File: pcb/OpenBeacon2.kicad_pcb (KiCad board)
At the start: 2 copper layers, 100 x 80 mm, 89 parts, among them J1 Bias V, J10 UART, J11 BNC, J2 PAI+, J3 PAI-, J4 Digital IO, J5 ADC Inputs, J6 SMA, J8 I2C Bus, J9 GND, K1 G5V-1-DC5, K2 G5V-1-DC5, M1 LPF 1, M2 LPF 2, Q1 2N7002, Q2 MMBT4403, Q3 2SK3074, Q4 2N7002, Q5 2N7002, Q6 2N7002, U1 TLV61046A, U2 ASTX-H11-25.000MHZ-T, U3 SN74LVC1G17, U4 SI5351A, U5 MCP4725A1T-E/CH, U6 128x32 OLED, U7 Empyrean, U8 24AA64T

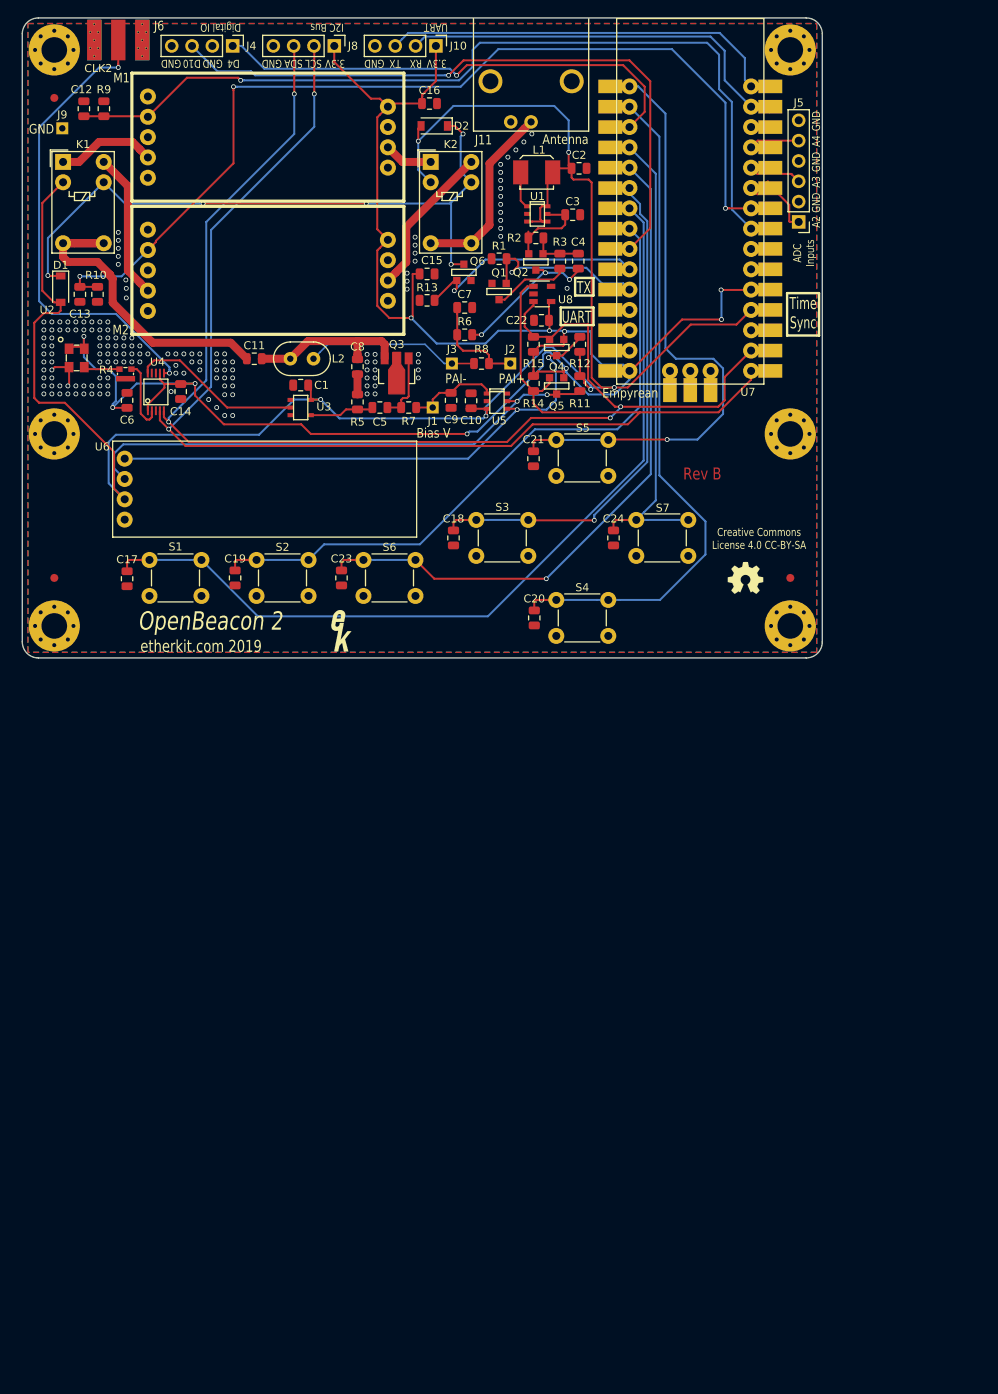
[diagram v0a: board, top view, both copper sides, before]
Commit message: PCB layout pass 1: 100x120 4L outline, JLC 7628 stackup, VFO-pattern mounting holes, placement (no routing)
- Board rebuilt from the merged KiCad 10 schematic (0406853); old KiCad 5 rev B board replaced
- Stackup/rules/RF50 netclass (0.31 mm CPWG, 0.20 gap) from Si5351AVFO pcb-layout
- DS1, S1/S2/S6 at VFO rev4 DS1/SW2/SW3/SW4 positions (+55 mm Y); D-pad cross at VFO encoder area
- RF chain: Si5351/TCXO -> BS170 PA -> K1-K3 -> F2-F5 T30 columns -> K4-K6 -> J11 BNC (right edge)
- CR1220 footprint: locating holes changed to NPTH (were zero-annulus PTH)
- DRC: 0 errors, 0 parity issues; unrouted nets + silkscreen warnings only
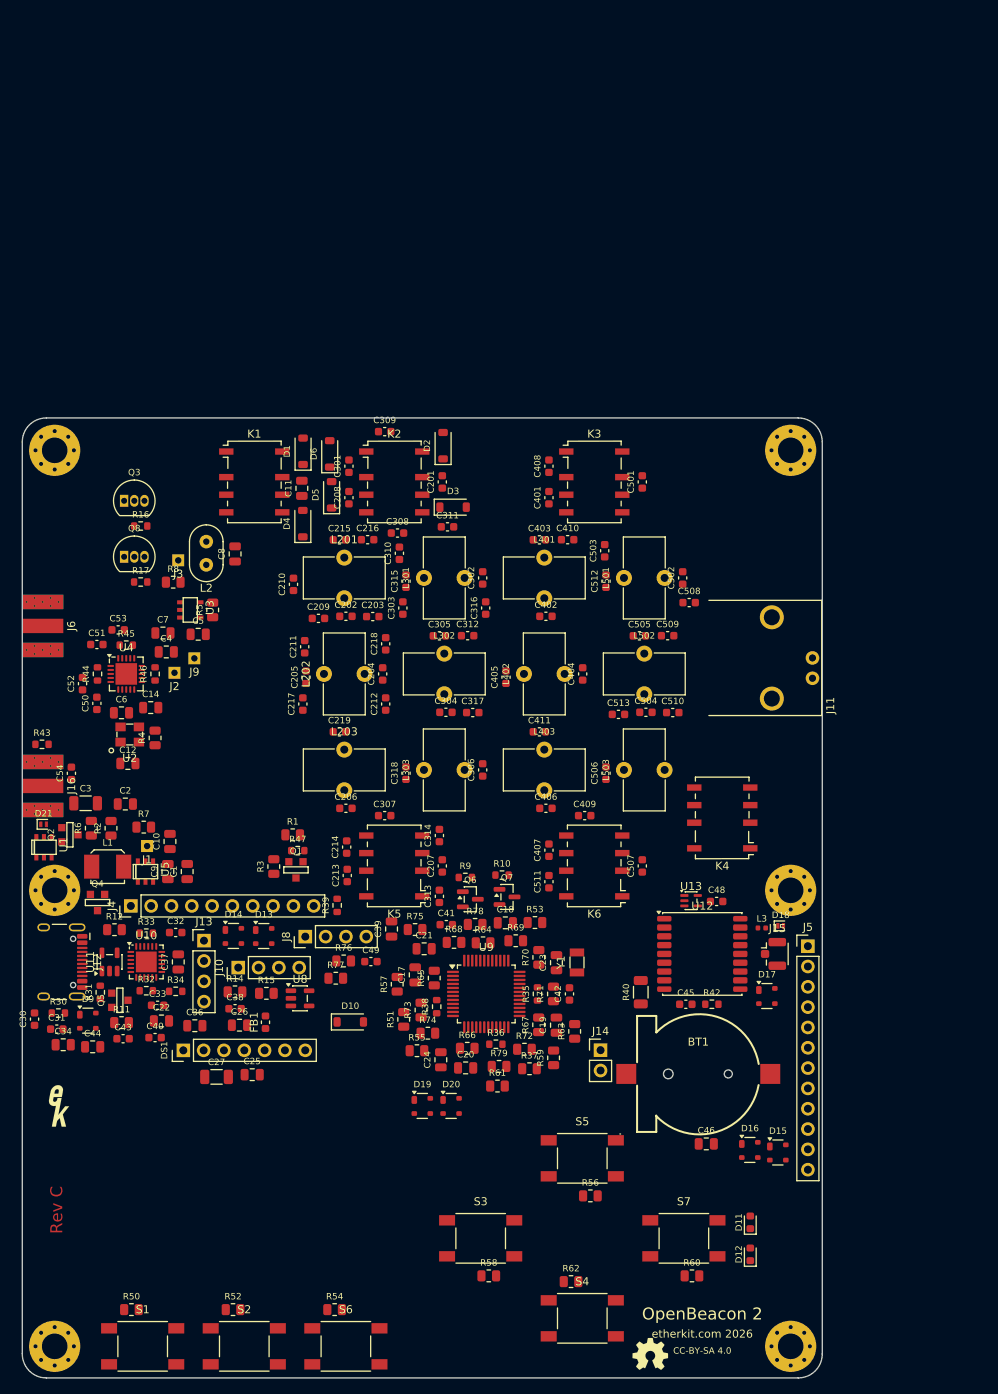
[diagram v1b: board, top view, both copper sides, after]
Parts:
- removed C13: 100n, Capacitor_SMD:C_0805_2012Metric
- removed C15, C16: 4.7u, Capacitor_SMD:C_0805_2012Metric
- removed G***: LOGO, EtherkitKicadLibrary:OSHWLogo4mm
- removed M1: LPF 1, EtherkitKicadLibrary:LPFModule
- removed M2: LPF 2, EtherkitKicadLibrary:LPFModule
- removed R13: 22k, Resistor_SMD:R_0805_2012Metric
- removed REF** (x3): Fiducial_1mm_Dia_2.54mm_Outer_CopperTop, Fiducial:Fiducial_1mm_Dia_2.54mm_Outer_CopperTop
- removed REF** (x6): MountingHole_3.2mm_M3_Pad_Via, MountingHole:MountingHole_3.2mm_M3_Pad_Via
- removed Ref**: Val**, EtherkitKicadLibrary:EtherkitLogoSmall
- removed U6: 128x32 OLED, EtherkitKicadLibrary:128x32OLED
- removed U7: Empyrean, EtherkitKicadLibrary:Empyrean
- added BT1: CR1220, OB2:BAT-SMD_KH-CR1220-2, F.Cu at (184.5, 182.0)
- added C201: 8.2p, Capacitor_SMD:C_0603_1608Metric, F.Cu at (152.5, 108.0)
- added C202: 68p, Capacitor_SMD:C_0603_1608Metric, F.Cu at (140.5, 124.8)
- added C203: 56p, Capacitor_SMD:C_0603_1608Metric, F.Cu at (143.8, 124.8)
- added C204: 100p, Capacitor_SMD:C_0603_1608Metric, F.Cu at (145.1, 132.0)
- added C205: 330p, Capacitor_SMD:C_0603_1608Metric, F.Cu at (135.5, 132.4)
- added C206: 18p, Capacitor_SMD:C_0603_1608Metric, F.Cu at (140.5, 148.8)
- added C207: 100p, Capacitor_SMD:C_0603_1608Metric, F.Cu at (152.5, 156.0)
- added C208: 330p, Capacitor_SMD:C_0603_1608Metric, F.Cu at (140.8, 110.0)
- added C209: 330p, Capacitor_SMD:C_0603_1608Metric, F.Cu at (137.0, 125.1)
- added C210: 330p, Capacitor_SMD:C_0603_1608Metric, F.Cu at (133.9, 120.8)
- added C211: 330p, Capacitor_SMD:C_0603_1608Metric, F.Cu at (135.3, 128.6)
- added C212: 330p, Capacitor_SMD:C_0603_1608Metric, F.Cu at (145.4, 135.8)
- added C213: 100p, Capacitor_SMD:C_0603_1608Metric, F.Cu at (140.6, 157.2)
- added C214: 330p, Capacitor_SMD:C_0603_1608Metric, F.Cu at (140.5, 153.6)
- added C215: 100p, Capacitor_SMD:C_0603_1608Metric, F.Cu at (139.6, 115.2)
- added C216: 330p, Capacitor_SMD:C_0603_1608Metric, F.Cu at (143.2, 115.2)
- added C217: 100p, Capacitor_SMD:C_0603_1608Metric, F.Cu at (135.1, 135.8)
- added C218: 100p, Capacitor_SMD:C_0603_1608Metric, F.Cu at (145.4, 128.2)
- added C219: 68p, Capacitor_SMD:C_0603_1608Metric, F.Cu at (139.6, 139.2)
- added C25: 4.7u, Capacitor_SMD:C_0805_2012Metric, F.Cu at (128.7, 182.1)
- added C26: 4.7u, Capacitor_SMD:C_0805_2012Metric, F.Cu at (127.2, 175.9)
- added C27: 22u, Capacitor_SMD:C_1206_3216Metric, F.Cu at (124.3, 182.4)
- added C30: 100n, Capacitor_SMD:C_0603_1608Metric, F.Cu at (101.5, 175.1)
- added C301: 100p, Capacitor_SMD:C_0603_1608Metric, F.Cu at (140.8, 106.0)
- added C302: 100p, Capacitor_SMD:C_0603_1608Metric, F.Cu at (157.6, 120.0)
- added C303: 56p, Capacitor_SMD:C_0603_1608Metric, F.Cu at (147.6, 123.8)
- added C304: 3p, Capacitor_SMD:C_0603_1608Metric, F.Cu at (153.0, 136.8)
- added C305: 330p, Capacitor_SMD:C_0603_1608Metric, F.Cu at (152.1, 127.2)
- added C306: 12p, Capacitor_SMD:C_0603_1608Metric, F.Cu at (157.6, 144.0)
- added C307: 56p, Capacitor_SMD:C_0603_1608Metric, F.Cu at (145.3, 149.7)
- added C308: 100p, Capacitor_SMD:C_0603_1608Metric, F.Cu at (146.9, 114.4)
- added C309: 100p, Capacitor_SMD:C_0603_1608Metric, F.Cu at (145.3, 101.7)
- added C31: 4.7u, Capacitor_SMD:C_0603_1608Metric, F.Cu at (104.3, 176.4)
- added C310: 100p, Capacitor_SMD:C_0603_1608Metric, F.Cu at (147.1, 116.9)
- added C311: 330p, Capacitor_SMD:C_0603_1608Metric, F.Cu at (153.2, 113.6)
- added C312: 330p, Capacitor_SMD:C_0603_1608Metric, F.Cu at (155.7, 127.2)
- added C313: 100p, Capacitor_SMD:C_0603_1608Metric, F.Cu at (152.1, 159.8)
- added C314: 330p, Capacitor_SMD:C_0603_1608Metric, F.Cu at (152.1, 152.2)
- added C315: 100p, Capacitor_SMD:C_0603_1608Metric, F.Cu at (148.0, 120.4)
- added C316: 100p, Capacitor_SMD:C_0603_1608Metric, F.Cu at (157.9, 123.8)
- added C317: 330p, Capacitor_SMD:C_0603_1608Metric, F.Cu at (156.3, 136.8)
- added C318: 68p, Capacitor_SMD:C_0603_1608Metric, F.Cu at (148.0, 144.4)
- added C32: 100n, Capacitor_SMD:C_0603_1608Metric, F.Cu at (119.2, 164.3)
- added C33: 4.7u, Capacitor_SMD:C_0603_1608Metric, F.Cu at (116.9, 173.4)
- added C34: 1u, Capacitor_SMD:C_0805_2012Metric, F.Cu at (105.1, 178.4)
- added C36: 4.7u, Capacitor_SMD:C_0805_2012Metric, F.Cu at (121.6, 176.0)
- added C37: 100n, Capacitor_SMD:C_0805_2012Metric, F.Cu at (119.5, 168.0)
- added C38: 100n, Capacitor_SMD:C_0603_1608Metric, F.Cu at (126.6, 173.8)
- added C39: 1u, Capacitor_SMD:C_0805_2012Metric, F.Cu at (146.2, 163.9)
- added C40: 100n, Capacitor_SMD:C_0603_1608Metric, F.Cu at (116.6, 177.5)
- added C401: 33p, Capacitor_SMD:C_0603_1608Metric, F.Cu at (165.8, 110.0)
- added C402: 6p, Capacitor_SMD:C_0603_1608Metric, F.Cu at (165.5, 124.8)
- added C403: 330p, Capacitor_SMD:C_0603_1608Metric, F.Cu at (164.6, 115.2)
- added C404: 68p, Capacitor_SMD:C_0603_1608Metric, F.Cu at (170.1, 132.0)
- added C405: 330p, Capacitor_SMD:C_0603_1608Metric, F.Cu at (160.5, 132.4)
- added C406: 3p, Capacitor_SMD:C_0603_1608Metric, F.Cu at (165.5, 148.8)
- added C407: 56p, Capacitor_SMD:C_0603_1608Metric, F.Cu at (165.8, 154.0)
- added C408: 100p, Capacitor_SMD:C_0603_1608Metric, F.Cu at (165.8, 106.0)
- added C409: 100p, Capacitor_SMD:C_0603_1608Metric, F.Cu at (170.3, 149.7)
- added C41: 15p, Capacitor_SMD:C_0603_1608Metric, F.Cu at (153.0, 163.3)
- added C410: 100p, Capacitor_SMD:C_0603_1608Metric, F.Cu at (168.2, 115.2)
- added C411: 68p, Capacitor_SMD:C_0603_1608Metric, F.Cu at (164.6, 139.2)
- added C42: 15p, Capacitor_SMD:C_0603_1608Metric, F.Cu at (168.4, 172.0)
- added C43: 100n, Capacitor_SMD:C_0603_1608Metric, F.Cu at (112.6, 177.6)
- added C44: 4.7u, Capacitor_SMD:C_0805_2012Metric, F.Cu at (108.8, 178.6)
- added C45: 10n, Capacitor_SMD:C_0603_1608Metric, F.Cu at (182.9, 173.3)
- added C46: 1u, Capacitor_SMD:C_0805_2012Metric, F.Cu at (185.5, 190.7)
- added C48: 100n, Capacitor_SMD:C_0603_1608Metric, F.Cu at (186.8, 160.4)
- added C49: 100n, Capacitor_SMD:C_0603_1608Metric, F.Cu at (143.6, 168.0)
- added C50: 100n, Capacitor_SMD:C_0603_1608Metric, F.Cu at (109.3, 135.7)
- added C501: 68p, Capacitor_SMD:C_0603_1608Metric, F.Cu at (177.5, 108.0)
- added C502: 56p, Capacitor_SMD:C_0603_1608Metric, F.Cu at (182.6, 120.0)
- added C503: 68p, Capacitor_SMD:C_0603_1608Metric, F.Cu at (172.8, 116.6)
- added C504: 6.8p, Capacitor_SMD:C_0603_1608Metric, F.Cu at (178.0, 136.8)
- added C505: 22p, Capacitor_SMD:C_0603_1608Metric, F.Cu at (177.1, 127.2)
- added C506: 22p, Capacitor_SMD:C_0603_1608Metric, F.Cu at (173.0, 144.4)
- added C507: 33p, Capacitor_SMD:C_0603_1608Metric, F.Cu at (177.5, 156.0)
- added C508: 100p, Capacitor_SMD:C_0603_1608Metric, F.Cu at (183.4, 123.1)
- added C509: 100p, Capacitor_SMD:C_0603_1608Metric, F.Cu at (180.7, 127.2)
- added C51: 100n, Capacitor_SMD:C_0603_1608Metric, F.Cu at (109.3, 128.3)
- added C510: 100p, Capacitor_SMD:C_0603_1608Metric, F.Cu at (181.3, 136.8)
- added C511: 100p, Capacitor_SMD:C_0603_1608Metric, F.Cu at (165.8, 158.0)
- added C512: 68p, Capacitor_SMD:C_0603_1608Metric, F.Cu at (173.0, 120.4)
- added C513: 68p, Capacitor_SMD:C_0603_1608Metric, F.Cu at (174.5, 137.1)
- added C52: 100n, Capacitor_SMD:C_0603_1608Metric, F.Cu at (107.5, 133.2)
- added C53: 100n, Capacitor_SMD:C_0603_1608Metric, F.Cu at (112.0, 126.5)
- added C54: 100n, Capacitor_SMD:C_0603_1608Metric, F.Cu at (106.1, 144.4)
- added D10: 1N5711W, Diode_SMD:D_SOD-123, F.Cu at (141.0, 175.5)
- added D11: SYNC, LED_SMD:LED_0603_1608Metric, F.Cu at (191.0, 200.6)
- added D12: TX, LED_SMD:LED_0603_1608Metric, F.Cu at (191.0, 204.6)
- added D13: SP0503BAHT, Package_TO_SOT_SMD:SOT-143, F.Cu at (130.2, 164.8)
- added D14: SP0503BAHT, Package_TO_SOT_SMD:SOT-143, F.Cu at (126.4, 164.8)
- added D15: SP0503BAHT, Package_TO_SOT_SMD:SOT-143, F.Cu at (194.4, 191.8)
- added D16: SP0503BAHT, Package_TO_SOT_SMD:SOT-143, F.Cu at (190.9, 191.5)
- added D17: SP0503BAHT, Package_TO_SOT_SMD:SOT-143, F.Cu at (193.1, 172.3)
- added D18: PESD5V0F1BL, Diode_SMD:D_SOD-882, F.Cu at (194.8, 163.5)
- added D19: SP0503BAHT, Package_TO_SOT_SMD:SOT-143, F.Cu at (150.0, 186.0)
- added D20: SP0503BAHT, Package_TO_SOT_SMD:SOT-143, F.Cu at (153.6, 186.0)
- added D21: PESD5V0F1BL, Diode_SMD:D_SOD-882, F.Cu at (102.7, 150.8)
- added D3: 1N4148W, Diode_SMD:D_SOD-123, F.Cu at (153.9, 111.2)
- added D4: 1N4148W, Diode_SMD:D_SOD-123, F.Cu at (135.1, 113.2)
- added D5: 1N4148W, Diode_SMD:D_SOD-123, F.Cu at (138.7, 109.6)
- added D6: 1N4148W, Diode_SMD:D_SOD-123, F.Cu at (138.4, 104.5)
- added D9: SP0503BAHT, Package_TO_SOT_SMD:SOT-143, F.Cu at (108.2, 175.3)
- added DS1: OLED_1.3in_SH1106_SPI_7pin, Connector_PinHeader_2.54mm:PinHeader_1x07_P2.54mm_Vertical, F.Cu at (120.1, 179.1)
- added FB1: BLM18PG221, Inductor_SMD:L_0603_1608Metric, F.Cu at (130.4, 175.5)
- added H1: MountingHole_M3, MountingHole:MountingHole_3.2mm_M3_Pad_Via, F.Cu at (104.0, 159.1)
- added H2: MountingHole_M3, MountingHole:MountingHole_3.2mm_M3_Pad_Via, F.Cu at (196.1, 159.1)
- added H3: MountingHole_M3, MountingHole:MountingHole_3.2mm_M3_Pad_Via, F.Cu at (104.0, 216.1)
- added H4: MountingHole_M3, MountingHole:MountingHole_3.2mm_M3_Pad_Via, F.Cu at (196.1, 216.1)
- added H5: MountingHole_M3, MountingHole:MountingHole_3.2mm_M3_Pad_Via, F.Cu at (104.0, 104.0)
- added H6: MountingHole_M3, MountingHole:MountingHole_3.2mm_M3_Pad_Via, F.Cu at (196.1, 104.0)
- added J12: USB_C_Receptacle, Connector_USB:USB_C_Receptacle_HCTL_HC-TYPE-C-16P-01A, F.Cu at (103.8, 168.0)
- added J13: UPDI, Connector_PinHeader_2.54mm:PinHeader_1x04_P2.54mm_Vertical, F.Cu at (122.7, 165.3)
- added J14: PPS, Connector_PinHeader_2.54mm:PinHeader_1x02_P2.54mm_Vertical, F.Cu at (172.3, 179.0)
- added J15: U.FL, Connector_Coaxial:U.FL_Hirose_U.FL-R-SMT-1_Vertical, F.Cu at (194.4, 167.0)
- added J16: SMA CLKIN, OB2:SMA-ENDLAUNCH, F.Cu at (100.0, 146.0)
- added K3: G6K-2F-Y-DC5, Relay_SMD:Relay_DPDT_Omron_G6K-2F-Y, F.Cu at (171.5, 108.0)
- added K4: G6K-2F-Y-DC5, Relay_SMD:Relay_DPDT_Omron_G6K-2F-Y, F.Cu at (187.5, 150.0)
- added K5: G6K-2F-Y-DC5, Relay_SMD:Relay_DPDT_Omron_G6K-2F-Y, F.Cu at (146.5, 156.0)
- added K6: G6K-2F-Y-DC5, Relay_SMD:Relay_DPDT_Omron_G6K-2F-Y, F.Cu at (171.5, 156.0)
- added L201: 1.10u, Inductor_THT:L_Toroid_Vertical_L10.0mm_W5.0mm_P5.08mm, F.Cu at (140.2, 117.5)
- added L202: 1.55u, Inductor_THT:L_Toroid_Vertical_L10.0mm_W5.0mm_P5.08mm, F.Cu at (137.7, 132.0)
- added L203: 1.90u, Inductor_THT:L_Toroid_Vertical_L10.0mm_W5.0mm_P5.08mm, F.Cu at (140.2, 141.5)
- added L3: 27nH, Inductor_SMD:L_0402_1005Metric, F.Cu at (192.4, 163.8)
- added L301: 430n, Inductor_THT:L_Toroid_Vertical_L10.0mm_W5.0mm_P5.08mm, F.Cu at (150.2, 120.0)
- added L302: 430n, Inductor_THT:L_Toroid_Vertical_L10.0mm_W5.0mm_P5.08mm, F.Cu at (152.8, 129.5)
- added L303: 619n, Inductor_THT:L_Toroid_Vertical_L10.0mm_W5.0mm_P5.08mm, F.Cu at (150.2, 144.0)
- added L401: 292n, Inductor_THT:L_Toroid_Vertical_L10.0mm_W5.0mm_P5.08mm, F.Cu at (165.2, 117.5)
- added L402: 360n, Inductor_THT:L_Toroid_Vertical_L10.0mm_W5.0mm_P5.08mm, F.Cu at (162.7, 132.0)
- added L403: 360n, Inductor_THT:L_Toroid_Vertical_L10.0mm_W5.0mm_P5.08mm, F.Cu at (165.2, 141.5)
- added L501: 130n, Inductor_THT:L_Toroid_Vertical_L10.0mm_W5.0mm_P5.08mm, F.Cu at (175.2, 120.0)
- added L502: 176n, Inductor_THT:L_Toroid_Vertical_L10.0mm_W5.0mm_P5.08mm, F.Cu at (177.8, 129.5)
- added L503: 230n, Inductor_THT:L_Toroid_Vertical_L10.0mm_W5.0mm_P5.08mm, F.Cu at (175.2, 144.0)
- added LOGO1: LOGO, EtherkitKicadLibrary:EtherkitLogoSmall, F.Cu at (104.6, 186.0)
- added LOGO2: LOGO, EtherkitKicadLibrary:OSHWLogo4mm, F.Cu at (178.5, 217.0)
- added Q7: AO3400A, Package_TO_SOT_SMD:SOT-23, F.Cu at (160.6, 159.9)
- added Q8: BS170, Package_TO_SOT_THT:TO-92_Inline, F.Cu at (112.7, 117.4)
- added R16: 10, Resistor_SMD:R_0603_1608Metric, F.Cu at (114.8, 113.5)
- added R17: 10, Resistor_SMD:R_0603_1608Metric, F.Cu at (114.8, 120.5)
- added R30: 5.1k, Resistor_SMD:R_0603_1608Metric, F.Cu at (104.5, 174.4)
- added R31: 5.1k, Resistor_SMD:R_0603_1608Metric, F.Cu at (109.7, 171.8)
- added R32: 1k, Resistor_SMD:R_0603_1608Metric, F.Cu at (115.5, 171.6)
- added R33: 22.1k, Resistor_SMD:R_0603_1608Metric, F.Cu at (115.5, 164.4)
- added R34: 47.5k, Resistor_SMD:R_0603_1608Metric, F.Cu at (119.2, 171.7)
- added R35: 470, Resistor_SMD:R_0603_1608Metric, F.Cu at (164.4, 172.0)
- added R36: 1k, Resistor_SMD:R_0603_1608Metric, F.Cu at (159.2, 178.3)
- added R37: 10k, Resistor_SMD:R_0805_2012Metric, F.Cu at (163.4, 181.4)
- added R38: 470, Resistor_SMD:R_0603_1608Metric, F.Cu at (151.8, 173.6)
- added R39: 470, Resistor_SMD:R_0603_1608Metric, F.Cu at (139.4, 160.9)
- added R40: 10R, Resistor_SMD:R_1206_3216Metric, F.Cu at (177.3, 171.8)
- added R42: 470, Resistor_SMD:R_0603_1608Metric, F.Cu at (186.2, 173.3)
- added R43: 49.9, Resistor_SMD:R_0603_1608Metric, F.Cu at (102.5, 140.8)
- added R44: 10k, Resistor_SMD:R_0603_1608Metric, F.Cu at (109.4, 132.0)
- added R45: 10k, Resistor_SMD:R_0603_1608Metric, F.Cu at (113.0, 128.4)
- added R46: 10k, Resistor_SMD:R_0603_1608Metric, F.Cu at (116.6, 132.0)
- added R47: 33, Resistor_SMD:R_0603_1608Metric, F.Cu at (134.4, 154.1)
- added R50: 10k, Resistor_SMD:R_0805_2012Metric, F.Cu at (113.6, 211.5)
- added R51: 10k, Resistor_SMD:R_0805_2012Metric, F.Cu at (147.7, 175.2)
- added R52: 10k, Resistor_SMD:R_0805_2012Metric, F.Cu at (126.3, 211.5)
- added R53: 10k, Resistor_SMD:R_0805_2012Metric, F.Cu at (164.1, 163.1)
- added R54: 10k, Resistor_SMD:R_0805_2012Metric, F.Cu at (139.0, 211.5)
- added R55: 10k, Resistor_SMD:R_0805_2012Metric, F.Cu at (149.3, 179.1)
- added R56: 10k, Resistor_SMD:R_0805_2012Metric, F.Cu at (171.0, 197.2)
- added R57: 10k, Resistor_SMD:R_0805_2012Metric, F.Cu at (146.9, 170.8)
- added R58: 10k, Resistor_SMD:R_0805_2012Metric, F.Cu at (158.3, 207.2)
- added R59: 10k, Resistor_SMD:R_0805_2012Metric, F.Cu at (166.4, 180.0)
- added R60: 10k, Resistor_SMD:R_0805_2012Metric, F.Cu at (183.7, 207.2)
- added R61: 10k, Resistor_SMD:R_0805_2012Metric, F.Cu at (159.4, 183.5)
- added R62: 10k, Resistor_SMD:R_0805_2012Metric, F.Cu at (168.6, 208.0)
- added R63: 10k, Resistor_SMD:R_0805_2012Metric, F.Cu at (169.0, 176.7)
- added R64: 220R, Resistor_SMD:R_0805_2012Metric, F.Cu at (157.6, 165.6)
- added R65: 220R, Resistor_SMD:R_0805_2012Metric, F.Cu at (151.5, 170.0)
- added R66: 220R, Resistor_SMD:R_0805_2012Metric, F.Cu at (155.6, 178.8)
- added R67: 220R, Resistor_SMD:R_0805_2012Metric, F.Cu at (164.5, 175.9)
- added R68: 220R, Resistor_SMD:R_0805_2012Metric, F.Cu at (154.0, 165.6)
- added R69: 220R, Resistor_SMD:R_0805_2012Metric, F.Cu at (161.7, 165.4)
- added R70: 220R, Resistor_SMD:R_0805_2012Metric, F.Cu at (164.6, 167.4)
- added R71: 220R, Resistor_SMD:R_0805_2012Metric, F.Cu at (166.4, 172.0)
- added R72: 220R, Resistor_SMD:R_0805_2012Metric, F.Cu at (162.8, 178.9)
- added R73: 220R, Resistor_SMD:R_0805_2012Metric, F.Cu at (149.8, 174.0)
- added R74: 220R, Resistor_SMD:R_0805_2012Metric, F.Cu at (150.7, 176.9)
- added R75: 220R, Resistor_SMD:R_0805_2012Metric, F.Cu at (149.1, 164.0)
- added R76: 220R, Resistor_SMD:R_0805_2012Metric, F.Cu at (140.2, 167.9)
- added R77: 220R, Resistor_SMD:R_0805_2012Metric, F.Cu at (139.2, 170.0)
- added R78: 220R, Resistor_SMD:R_0805_2012Metric, F.Cu at (156.6, 163.3)
- added R79: 220R, Resistor_SMD:R_0805_2012Metric, F.Cu at (159.6, 181.1)
- added U10: CP2102N-A02-GQFN24, Package_DFN_QFN:QFN-24-1EP_4x4mm_P0.5mm_EP2.6x2.6mm, F.Cu at (115.5, 168.0)
- added U11: TLV75533PDBV, Package_TO_SOT_SMD:SOT-23-5, F.Cu at (110.9, 168.0)
- added U12: MAX-M10S-00B, RF_GPS:ublox_MAX, F.Cu at (185.0, 167.0)
- added U13: TPS22941, Package_TO_SOT_SMD:SOT-353_SC-70-5, F.Cu at (183.6, 160.3)
- added U9: AVR128DA48-E/PT, Package_QFP:TQFP-48_7x7mm_P0.5mm, F.Cu at (158.0, 172.0)
- added Y1: 32.768kHz, Crystal:Crystal_SMD_3215-2Pin_3.2x1.5mm, F.Cu at (169.3, 168.1)
- C2: value 2.2u -> 4.7u
- C3: footprint Capacitor_SMD:C_0805_2012Metric -> Capacitor_SMD:C_1206_3216Metric
- J4: footprint Connector_PinHeader_2.54mm:PinHeader_1x04_P2.54mm_Vertical -> Connector_PinHeader_2.54mm:PinHeader_1x10_P2.54mm_Vertical
- J5: footprint Connector_PinHeader_2.54mm:PinHeader_1x06_P2.54mm_Vertical -> Connector_PinHeader_2.54mm:PinHeader_1x12_P2.54mm_Vertical
- J6: footprint EtherkitKicadLibrary:SMA-ENDLAUNCH -> OB2:SMA-ENDLAUNCH
- K1, K2: value G5V-1-DC5 -> G6K-2F-Y-DC5; footprint Relay_THT:Relay_SPDT_Omron_G5V-1 -> Relay_SMD:Relay_DPDT_Omron_G6K-2F-Y
- L1: value FDSD0420-H-100M-P3 -> MWSA0402S-100MT
- Q3: value 2SK3074 -> BS170; footprint EtherkitKicadLibrary:SOT89-3 -> Package_TO_SOT_THT:TO-92_Inline
- Q6: value 2N7002 -> AO3400A; footprint EtherkitKicadLibrary:SOT23-2N7002 -> Package_TO_SOT_SMD:SOT-23
- R10, R9: value 270k -> 22k; footprint Resistor_SMD:R_0805_2012Metric -> Resistor_SMD:R_0603_1608Metric
- R4: value PAT1220-C-10dB -> 10; footprint EtherkitKicadLibrary:PAT1220 -> Resistor_SMD:R_0805_2012Metric
- S1, S2, S3, S4, S5, S6, S7: footprint EtherkitKicadLibrary:Omron_B3F-1052 -> OB2:SW_Push_6x6mm_SMD_KH-6X6X11H-STM
- U2: value ASTX-H11-25.000MHZ-T -> 25.000 MHz TCXO
- U4: value SI5351A -> SI5351C-B-GMR; footprint EtherkitKicadLibrary:MSOP-10 -> Package_DFN_QFN:QFN-20-1EP_4x4mm_P0.5mm_EP2.7x2.7mm
- moved J10 117.8 mm to (127.0, 168.7), turned to 90 degrees
- moved J8 111.4 mm to (135.4, 164.8), turned to 90 degrees
- moved J4 108.3 mm to (113.6, 161.0), turned to 90 degrees
- moved R9 106.2 mm to (155.4, 157.4), turned to 0 degrees
- moved L1 102.0 mm to (110.7, 156.1)
- moved U1 100.4 mm to (102.7, 153.7), turned to 0 degrees
- moved C22 99.6 mm to (117.4, 175.4), turned to 0 degrees
- moved R11 98.3 mm to (112.4, 175.6), turned to 0 degrees
- moved C2 97.6 mm to (112.9, 148.3)
- moved S6 96.2 mm to (140.4, 216.1)
- moved S2 96.2 mm to (127.8, 216.1)
- moved S1 96.1 mm to (115.0, 216.1), turned to 0 degrees
- moved C3 95.5 mm to (107.9, 148.2)
- moved Q5 94.2 mm to (112.2, 172.8), turned to 90 degrees
- moved R12 93.5 mm to (111.5, 164.0), turned to 0 degrees
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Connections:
- C11 pad 1: Net-(C11-Pad1) -> /Filter Bank/LPF_IN
- C11 pad 2: Net-(C11-Pad2) -> Net-(Q3-D)
- C12 pad 1: BAND_ID_1 -> Net-(U2-OUT)
- C12 pad 2: GND -> Net-(U4-XA)
- C5 pad 1: Net-(C5-Pad1) -> Net-(C5-~-Pad1)
- C6 pad 1: +3.3V -> Net-(U2-VDD)
- C8 pad 1: Net-(C11-Pad2) -> Net-(Q3-D)
- D1 pad 1: BAND_RELAY -> +5V
- D1 pad 2: +5V -> /Filter Bank/COIL_A
- D2 pad 1: BAND_RELAY -> +5V
- D2 pad 2: +5V -> /Filter Bank/COIL_B
- J10 pad 2: UART_RX -> /I/O + UI/HDR_RX
- J10 pad 3: UART_TX -> /I/O + UI/HDR_TX
- J11 pad 1: Net-(J11-Pad1) -> /Filter Bank/LPF_OUT
- J4 pad 1: D4 -> /I/O + UI/HDR_D7
- J4 pad 3: D10 -> /I/O + UI/HDR_D17
- J5 pad 1: A2 -> /I/O + UI/HDR_D22
- J5 pad 3: A3 -> /I/O + UI/HDR_D23
- J5 pad 5: A4 -> /I/O + UI/HDR_D24
- J6 pad 1: Net-(J6-Pad1) -> Net-(J6-In)
- J8 pad 2: SCL -> /I/O + UI/HDR_SCL
- J8 pad 3: SDA -> /I/O + UI/HDR_SDA
- K1 pad 1: Net-(K1-Pad1) -> +5V
- K1 pad 2: +5V -> /Filter Bank/P1_IN
- K1 pad 5: Net-(C11-Pad1) -> unconnected-(K1-Pad5)
- K1 pad 6: Net-(C11-Pad1) -> unconnected-(K1-Pad6)
- K2 pad 1: Net-(K2-Pad1) -> +5V
- K2 pad 2: +5V -> /Filter Bank/F80_60_IN
- K2 pad 5: Net-(J11-Pad1) -> unconnected-(K2-Pad5)
- K2 pad 6: Net-(J11-Pad1) -> unconnected-(K2-Pad6)
- L2 pad 2: Net-(C11-Pad2) -> Net-(Q3-D)
- Q3 pad 1: GND -> Net-(Q3-D)
- Q3 pad 2: Net-(C5-Pad1) -> Net-(Q3-G)
- Q3 pad 3: Net-(C11-Pad2) -> GND
- Q6 pad 1: GND -> BAND_A
- Q6 pad 2: BAND_SW -> GND
- Q6 pad 3: BAND_RELAY -> /Filter Bank/COIL_A
- R10 pad 1: BAND_ID_2 -> BAND_B
- R4 pad 1: Net-(R4-Pad1) -> +3.3V
- R4 pad 2: Net-(R4-Pad2) -> Net-(U2-VDD)
- R7 pad 1: Net-(C5-Pad1) -> Net-(C5-~-Pad1)
- R9 pad 1: BAND_ID_1 -> BAND_A
- S1 pad 1: BTN_DSP_1 -> GND
- S1 pad 2: BTN_DSP_1 -> Net-(R50-Pad2)
- S2 pad 2: GND -> Net-(R52-Pad2)
- S3 pad 1: BTN_LEFT -> GND
- S3 pad 2: BTN_LEFT -> Net-(R58-Pad2)
- S4 pad 2: GND -> Net-(R62-Pad2)
- S5 pad 2: GND -> Net-(R56-Pad2)
- S6 pad 2: GND -> Net-(R54-Pad2)
- S7 pad 2: GND -> Net-(R60-Pad2)
- U2 pad 1: +3.3V -> GND
- U2 pad 3: Net-(R4-Pad1) -> Net-(U2-OUT)
- U2 pad 4: +3.3V -> Net-(U2-VDD)
- U4 pad 1: +3.3V -> Net-(U4-XA)
- U4 pad 10: CLK0 -> +3.3V
- U4 pad 2: Net-(R4-Pad2) -> unconnected-(U4-XB-Pad2)
- U4 pad 3: Net-(U4-Pad3) -> SI_INTR
- U4 pad 6: Net-(J6-Pad1) -> Net-(U4-CLKIN)
- U4 pad 7: +3.3V -> GND
- U4 pad 8: GND -> unconnected-(U4-CLK3-Pad8)
- U4 pad 9: Net-(U4-Pad9) -> Net-(J6-In)
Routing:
- net +5V: track 245.2 -> 0.00 mm, vias 6 -> 0
- net +3.3V: track 240.6 -> 0.00 mm, vias 10 -> 0
- net SCL: track 171.3 -> 0.00 mm, vias 2 -> 0
- net SDA: track 162.5 -> 0.00 mm, vias 4 -> 0
- net BAND_ID_2: track 122.7 -> 0.00 mm, vias 3 -> 0
- net BTN_DSP_1: track 109.1 -> 0.00 mm
- net BAND_ID_1: track 108.8 -> 0.00 mm, vias 1 -> 0
- net BTN_BACK: track 85.7 -> 0.00 mm, vias 1 -> 0
- net BTN_DOWN: track 84.9 -> 0.00 mm
- net BAND_RELAY: track 82.7 -> 0.00 mm, vias 5 -> 0
- net D10: track 82.7 -> 0.00 mm, vias 1 -> 0
- net BTN_DSP_2: track 82.6 -> 0.00 mm
- net BTN_UP: track 75.6 -> 0.00 mm, vias 1 -> 0
- net SDA_5V: track 69.0 -> 0.00 mm, vias 2 -> 0
- net SCL_5V: track 66.5 -> 0.00 mm, vias 2 -> 0
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- removed copper zone on B.Cu, net GND
- removed copper zone on F.Cu, net GND
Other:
- board size 100 x 80 mm -> 100 x 120 mm
- copper layers 2 -> 4
- net class 50ohm removed
- net class Default removed
- rule pad_to_mask_clearance: 0.2 -> 0
- board text added: "1.3in SH1106 OLED (DS1) - module area: low-profile SMD only, no tall parts"
- board text added: "CC-BY-SA 4.0"
- board text added: "Controlled impedance 50 ohm, L1/L2, 0.31/0.20 (CPWG, RF50) per JLC calculator"
- board text added: "FAB NOTES: JLC04161H-7628 4L 1.6mm, 1oz outer"
- board text added: "Hand solder: J11, L2, Q3, Q8, toroids L201-L503, DS1"
- board text added: "OpenBeacon 2 - NT7S / Etherkit"
- board text added: "PA (Q3/Q8/L2): give drains a dedicated F.Cu+B.Cu heat-spread pour with via stitching (routing pass)"
- board text added: "Rev C"
- board text added: "etherkit.com 2026"
- board text removed: "3.3V"
- board text removed: "A2"
- board text removed: "A3"
- board text removed: "A4"
- board text removed: "ADC Inputs"
- board text removed: "Antenna"
- board text removed: "Bias V"
- board text removed: "CLK2"
- board text removed: "Creative Commons License 4.0 CC-BY-SA"
- board text removed: "D10"
- board text removed: "D4"
- board text removed: "Digital IO"
- board text removed: "Empyrean"
- board text removed: "GND"
- board text removed: "I2C Bus"
- board text removed: "PAI+"
- board text removed: "PAI-"
- board text removed: "RX"
- board text removed: "Rev B"
- board text removed: "SCL"
- board text removed: "SDA"
- board text removed: "TX"
- board text removed: "Time Sync"
- board text removed: "UART"
- board text removed: "etherkit.com 2019"

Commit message: PCB placement: J11 BNC on back edge at filter output, reversed filter bank flow, aligned/labelled header row
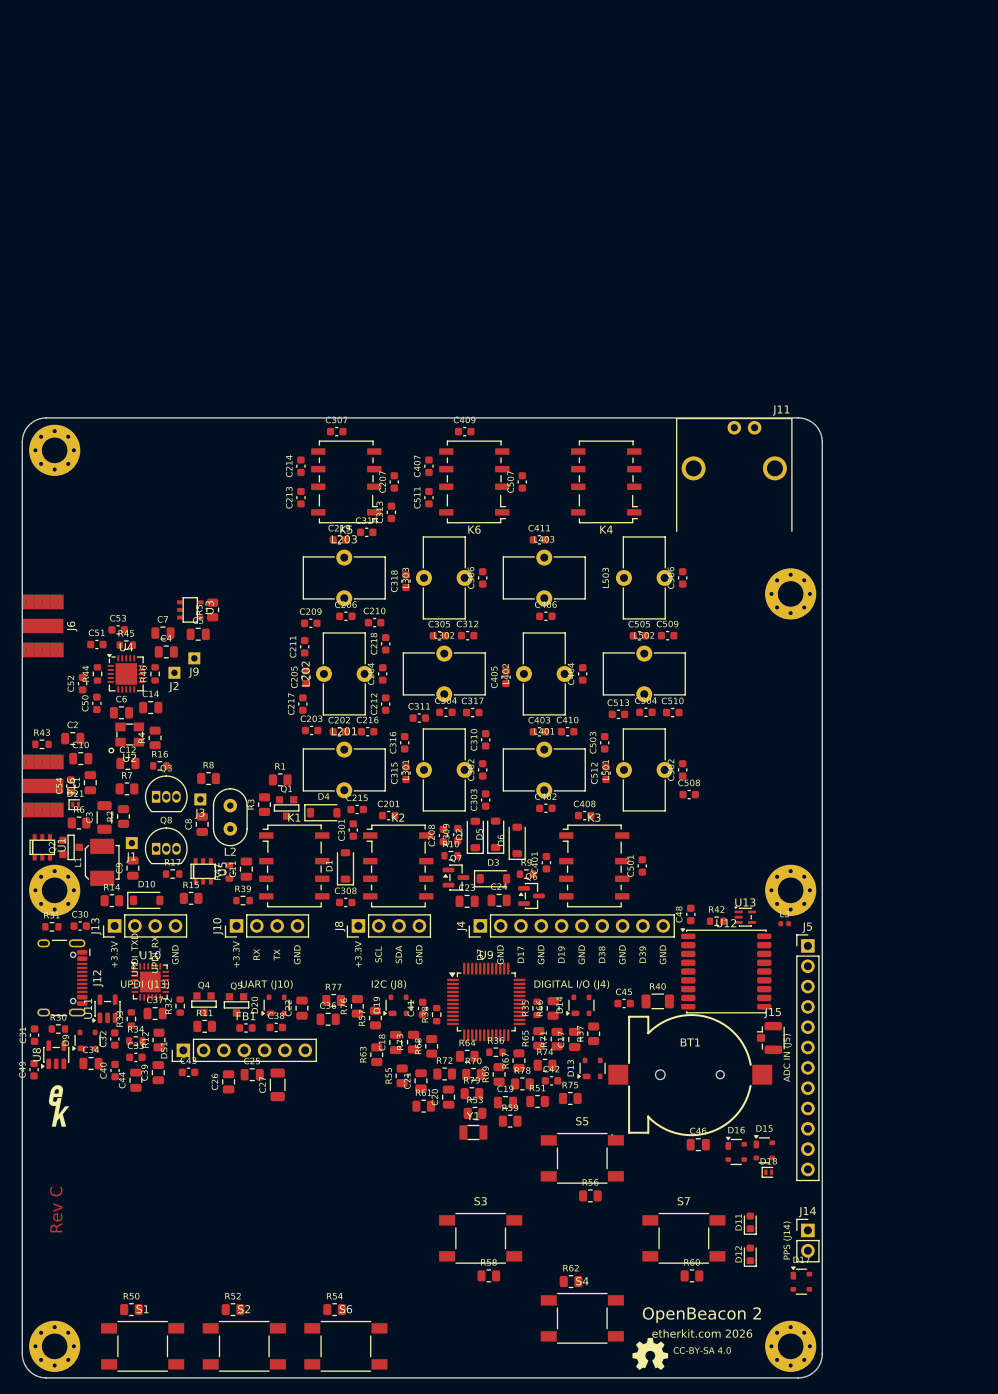
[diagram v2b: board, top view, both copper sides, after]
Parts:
- moved D6 53.7 mm to (161.9, 152.8)
- moved D1 52.1 mm to (140.4, 156.0)
- moved C309 51.2 mm to (154.4, 152.1), turned to 90 degrees
- moved C511 50.3 mm to (150.8, 110.0)
- moved C507 50.3 mm to (162.5, 108.0)
- moved K6 50.3 mm to (156.5, 108.0)
- moved C407 50.3 mm to (150.8, 106.0)
- moved C409 50.3 mm to (155.3, 101.7)
- moved D2 48.8 mm to (156.6, 152.1)
- moved C207 48.4 mm to (146.5, 108.0)
- moved C313 48.4 mm to (146.1, 111.8)
- moved K5 48.4 mm to (140.5, 108.0)
- moved C307 48.4 mm to (139.3, 101.7)
- moved K1 48.3 mm to (134.0, 156.0)
- moved C11 48.1 mm to (128.0, 156.4)
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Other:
- board text added: "+3.3V"
- board text added: "ADC IN (J5)"
- board text added: "D17"
- board text added: "D19"
- board text added: "D38"
- board text added: "D39"
- board text added: "D7"
- board text added: "DIGITAL I/O (J4)"
- board text added: "GND"
- board text added: "I2C (J8)"
- board text added: "PPS (J14)"
- board text added: "RX"
- board text added: "SCL"
- board text added: "SDA"
- board text added: "TX"
- board text added: "UART (J10)"
- board text added: "UPDI (J13)"
- board text added: "UPDI_RX"
- board text added: "UPDI_TXD"

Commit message: PCB Rev C re-place: 120x100 outline, back-edge J6/J16/J11/J12, BNC at filter-bank output, front-panel DS1/S1/S2/S6 + D-pad at VFO positions, header columns on 2.54 grid with labels
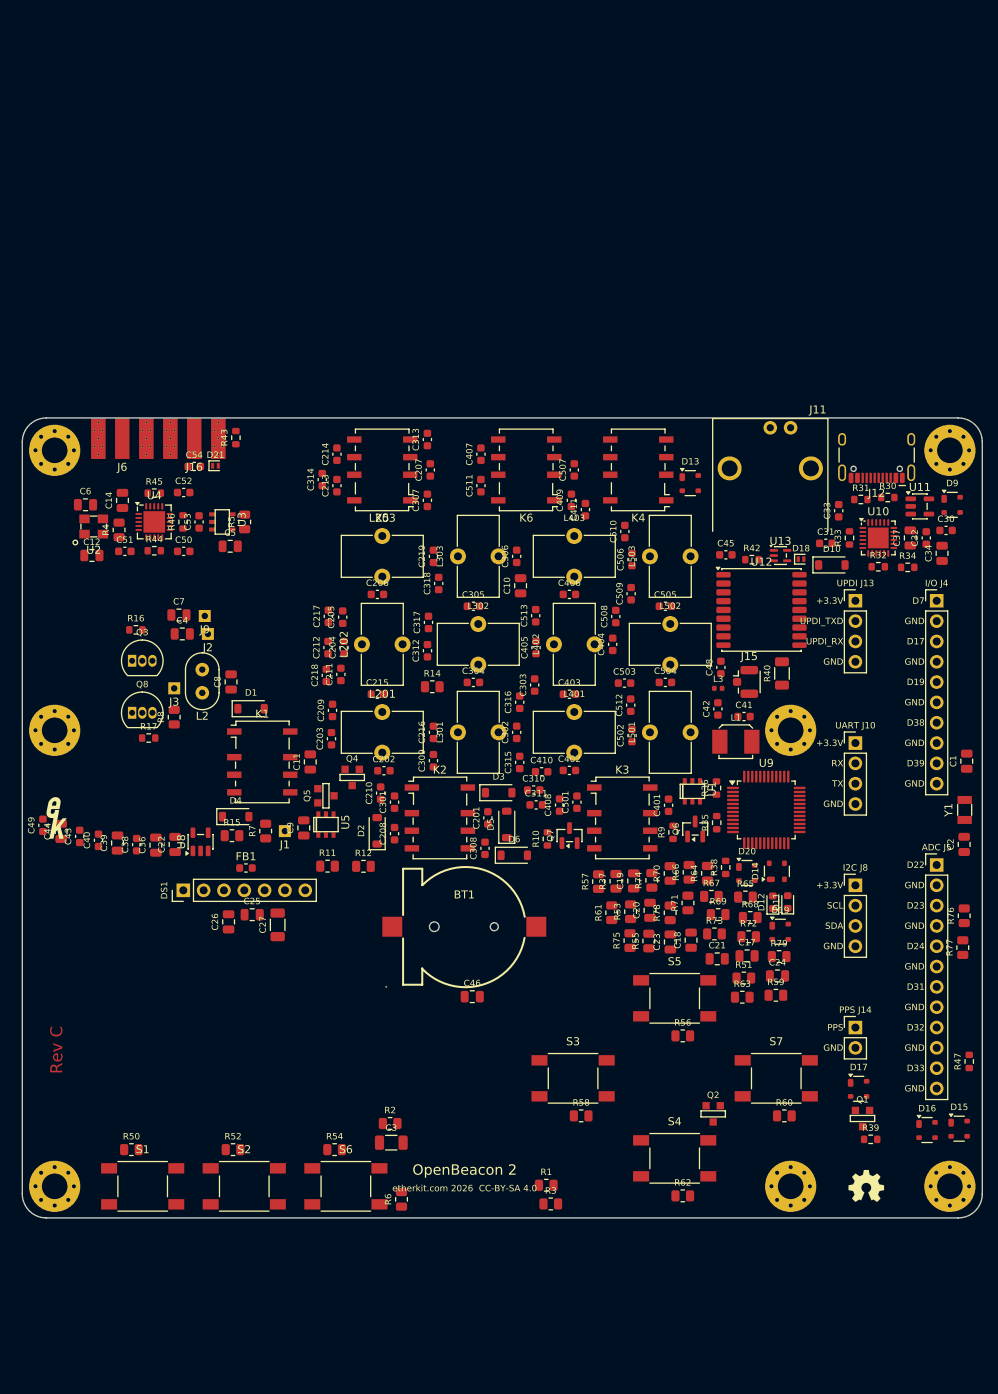
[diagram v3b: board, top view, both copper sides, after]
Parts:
- added H7: MountingHole_M3, MountingHole:MountingHole_3.2mm_M3_Pad_Via, F.Cu at (215.9, 196.1)
- moved D9 127.1 mm to (216.2, 110.9), turned to 0 degrees
- moved C34 124.0 mm to (215.0, 116.9), turned to 90 degrees
- moved R30 123.1 mm to (208.2, 109.9)
- moved J12 122.5 mm to (206.8, 103.8), turned to 180 degrees
- moved U11 119.4 mm to (212.2, 111.1), turned to 0 degrees
- moved C32 119.2 mm to (213.0, 115.0)
- moved C30 119.0 mm to (215.5, 114.1)
- moved C31 116.5 mm to (200.4, 115.7), turned to 0 degrees
- moved R31 114.4 mm to (204.8, 110.2)
- moved R34 113.2 mm to (210.7, 118.7)
- moved C2 112.2 mm to (217.7, 153.3), turned to 90 degrees
- moved C37 111.6 mm to (211.0, 115.0), turned to 90 degrees
- moved C33 111.3 mm to (202.1, 111.6), turned to 90 degrees
- moved C1 109.6 mm to (218.1, 142.9)
- moved R33 108.0 mm to (203.4, 115.0)
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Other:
- board size 100 x 120 mm -> 120 x 100 mm
- board text added: "1.3in SH1106 OLED (DS1) - module area: low-profile SMD only"
- board text added: "ADC J5"
- board text added: "D22"
- board text added: "D23"
- board text added: "D24"
- board text added: "D31"
- board text added: "D32"
- board text added: "D33"
- board text added: "I/O J4"
- board text added: "I2C J8"
- board text added: "OpenBeacon 2 - NT7S / Etherkit - Rev C"
- board text added: "PPS"
- board text added: "PPS J14"
- board text added: "UART J10"
- board text added: "UPDI J13"
- board text added: "etherkit.com 2026 CC-BY-SA 4.0"
- board text removed: "1.3in SH1106 OLED (DS1) - module area: low-profile SMD only, no tall parts"
- board text removed: "ADC IN (J5)"
- board text removed: "CC-BY-SA 4.0"
- board text removed: "DIGITAL I/O (J4)"
- board text removed: "I2C (J8)"
- board text removed: "OpenBeacon 2 - NT7S / Etherkit"
- board text removed: "PPS (J14)"
- board text removed: "UART (J10)"
- board text removed: "UPDI (J13)"
- board text removed: "etherkit.com 2026"
